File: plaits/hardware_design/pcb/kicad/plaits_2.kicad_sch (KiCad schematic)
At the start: 20 parts

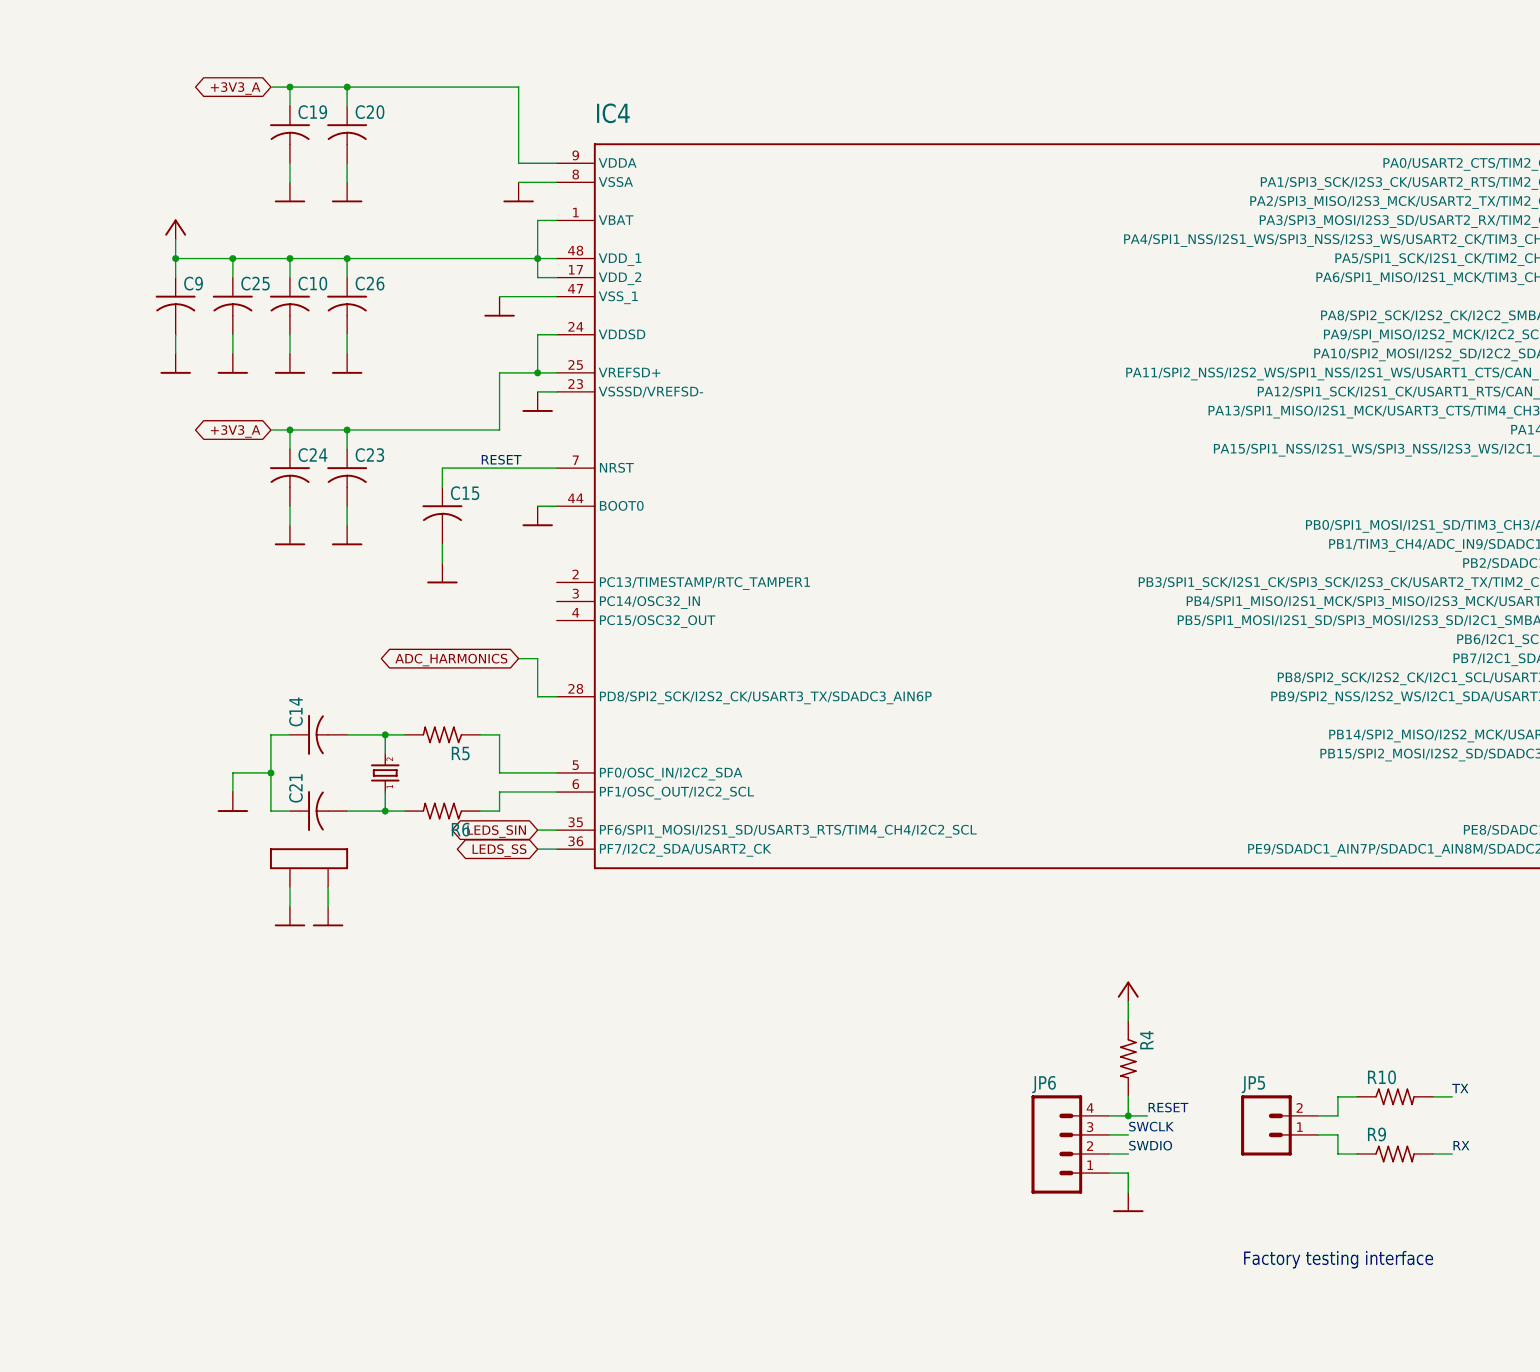
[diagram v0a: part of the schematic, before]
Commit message: plaits resized panasonic A -> B caps
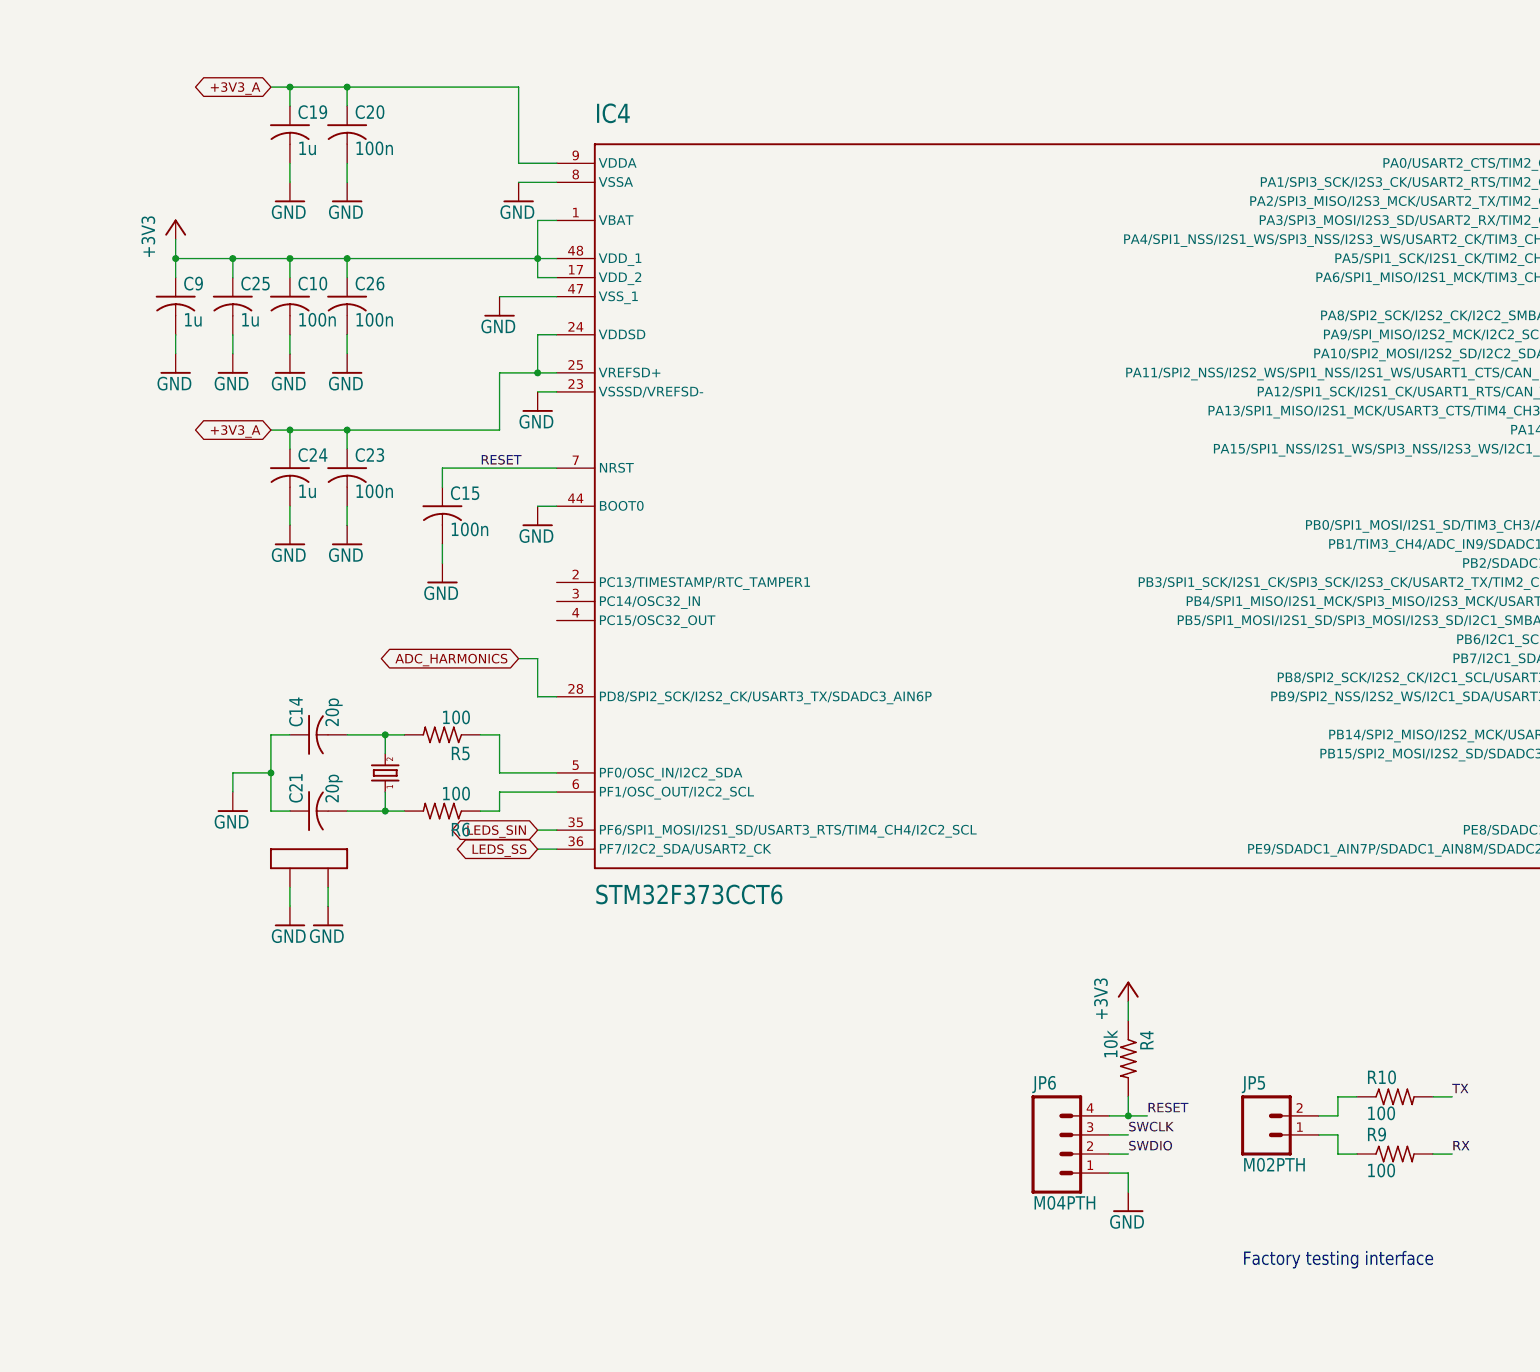
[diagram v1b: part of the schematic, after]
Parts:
- C10, C15, C20, C23, C26: value (none) -> 100n; footprint (none) -> plaits:C0402
- C14, C21: value (none) -> 20p; footprint (none) -> plaits:C0402
- C19, C24, C25, C9: value (none) -> 1u; footprint (none) -> plaits:C0402
- IC4: value (none) -> STM32F373CCT6; footprint (none) -> plaits:LQFP48
- JP5: value (none) -> M02PTH; footprint (none) -> plaits:1X02
- JP6: value (none) -> M04PTH; footprint (none) -> plaits:1X04
- Q1: value (none) -> 8MHz; footprint (none) -> plaits:CTS406
- R10, R5, R6, R9: value (none) -> 100; footprint (none) -> plaits:R0402
- R4: value (none) -> 10k; footprint (none) -> plaits:R0402
